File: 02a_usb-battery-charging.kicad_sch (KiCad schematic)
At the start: 22 parts, among them J5 USB4105-GF-A, J8 Conn_01x02_Socket, U3 BQ25170JDSGR

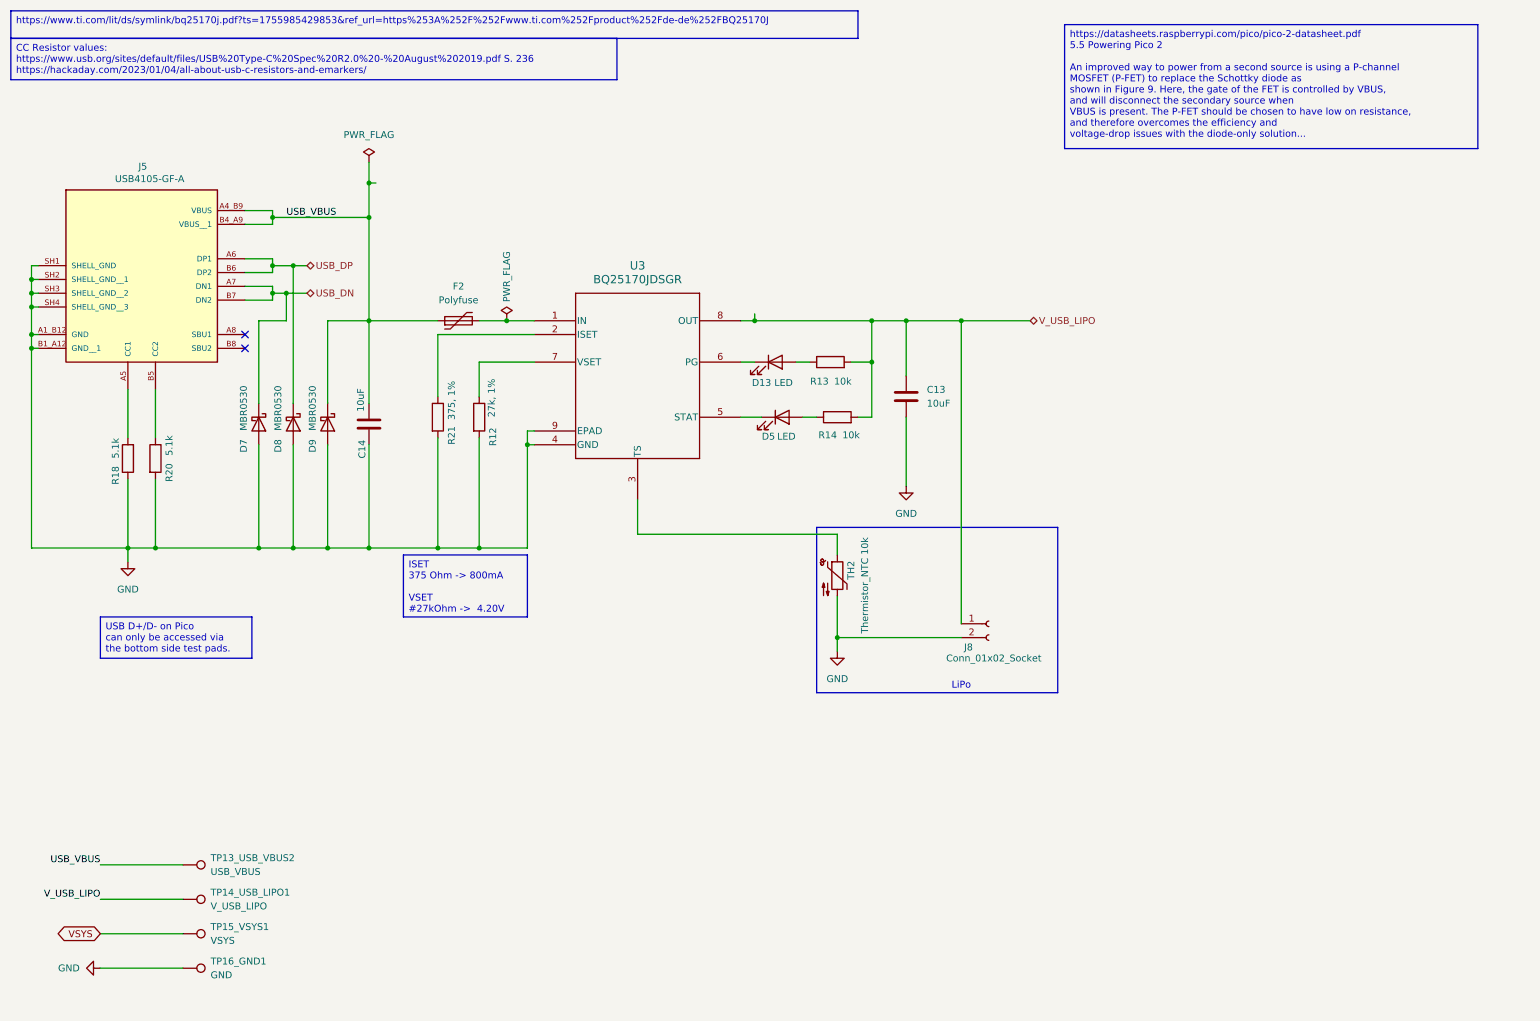
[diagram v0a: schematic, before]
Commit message: v2: major changes
- Move to hierarchical labels
- use another RP Pico Footprint
- split power path in USB/charging and on/off with a button approach in order to control turning on and off
  with the RP Pico, make use of long presses and delay turning of the voltage in order to do a proper shutdown
- introduce another charging controller with a better performance an a lower voltage needed in order to charge the battery
- rework display booster circuit
- rework SD and buttons
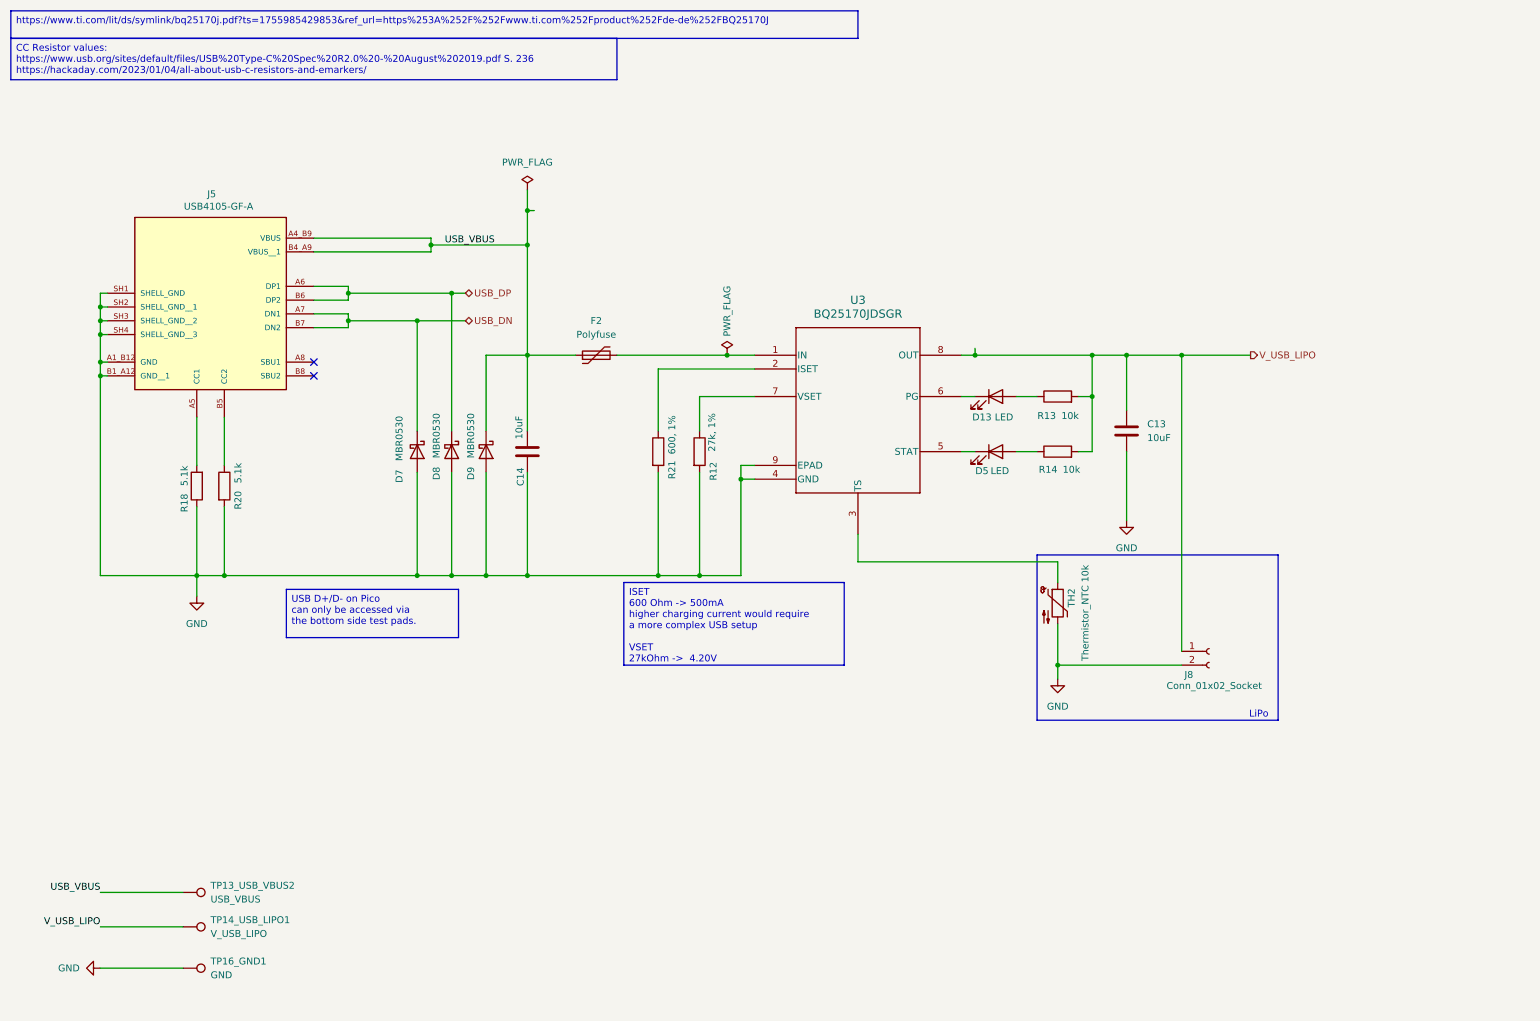
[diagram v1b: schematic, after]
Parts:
- removed TP15_VSYS1: VSYS, TestPoint:TestPoint_Pad_D2.5mm, symbol Connector:TestPoint
- F2: footprint (none) -> Resistor_SMD:R_1206_3216Metric_Pad1.30x1.75mm_HandSolder
- R21: value 375, 1% -> 600, 1%
- U3: footprint WSON8_BQ2517_TEX -> prj-footprints:WSON8_BQ2517_TEX
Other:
- moved on the sheet: C13, C14, D13, D5, D7, D8, D9, F2, J5, J8, R12, R13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

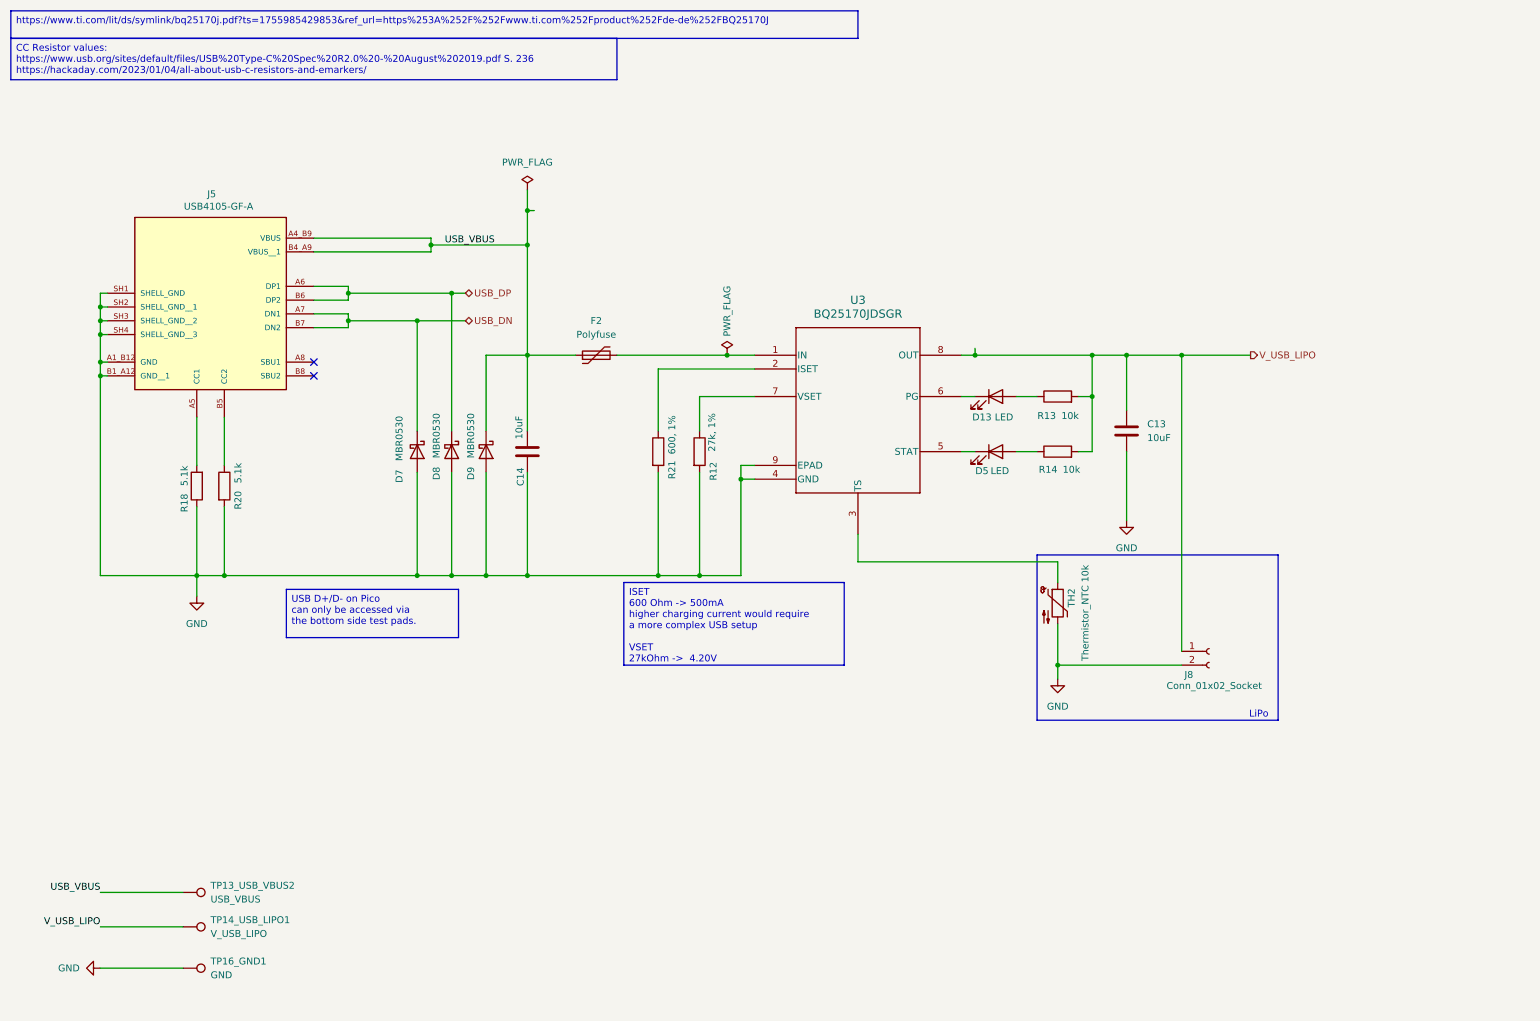
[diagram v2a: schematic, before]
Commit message: Reworked v2 routing
- some general improvements
- reworked component numbering
- routed and tuned differential pair (USB)
- added stiching vias and improved ground fills
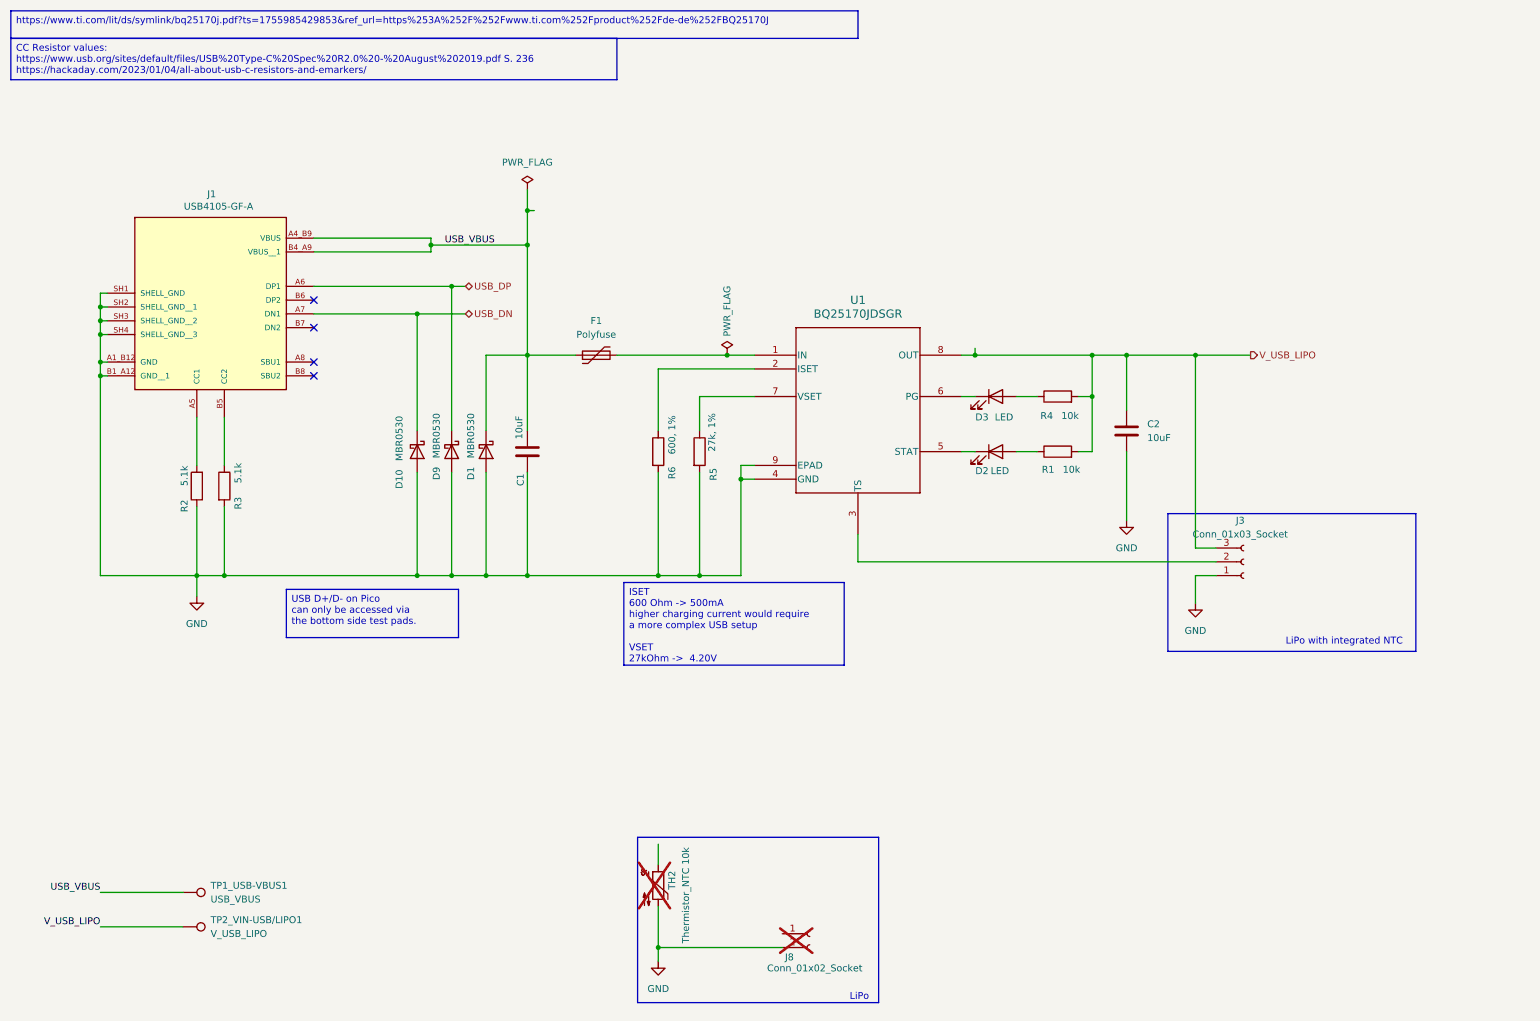
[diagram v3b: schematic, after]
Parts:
- removed TP16_GND1: GND, TestPoint:TestPoint_Pad_D2.5mm, symbol Connector:TestPoint
- added J3: Conn_01x03_Socket, Connector_JST:JST_PH_S3B-PH-K_1x03_P2.00mm_Horizontal, symbol Connector:Conn_01x03_Socket
- J8, TH2: now not fitted; now left out of the parts list
- renumbered C14 to C1, C13 to C2, D9 to D1, D7 to D10, D5 to D2, D13 to D3, D8 to D9, F2 to F1, J5 to J1, R14 to R1, R18 to R2, R20 to R3, R13 to R4, R12 to R5, R21 to R6, TP13_USB_VBUS2 to TP1_USB-VBUS1, TP14_USB_LIPO1 to TP2_VIN-USB/LIPO1, U3 to U1
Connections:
- net GND: now also J3.1 (Pin_1)
- net USB_DN: no longer J1.B7 (DN2)
- net USB_DP: no longer J1.B6 (DP2)
- net V_USB_LIPO: now also J3.3 (Pin_3); no longer J8.1 (Pin_1)
- net at TH2.1: no longer U1.3 (TS)
- new net: J3.2 (Pin_2), U1.3 (TS)
- no-connect marks 2 -> 4
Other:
- note added: "LiPo with integrated NTC"

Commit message: some minor improvements after evaluating the CI run
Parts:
- TP1_USB-VBUS1, TP2_VIN-USB/LIPO1: now left out of the parts list
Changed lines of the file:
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@@
 		(unit 1)
 		(exclude_from_sim no)
-		(in_bom yes)
+		(in_bom no)
 		(on_board yes)
 		(dnp no)
@@
 		(unit 1)
 		(exclude_from_sim no)
-		(in_bom yes)
-		(on_board yes)
-		(dnp no)
+		(in_bom no)
+		(on_board yes)
+		(dnp no)

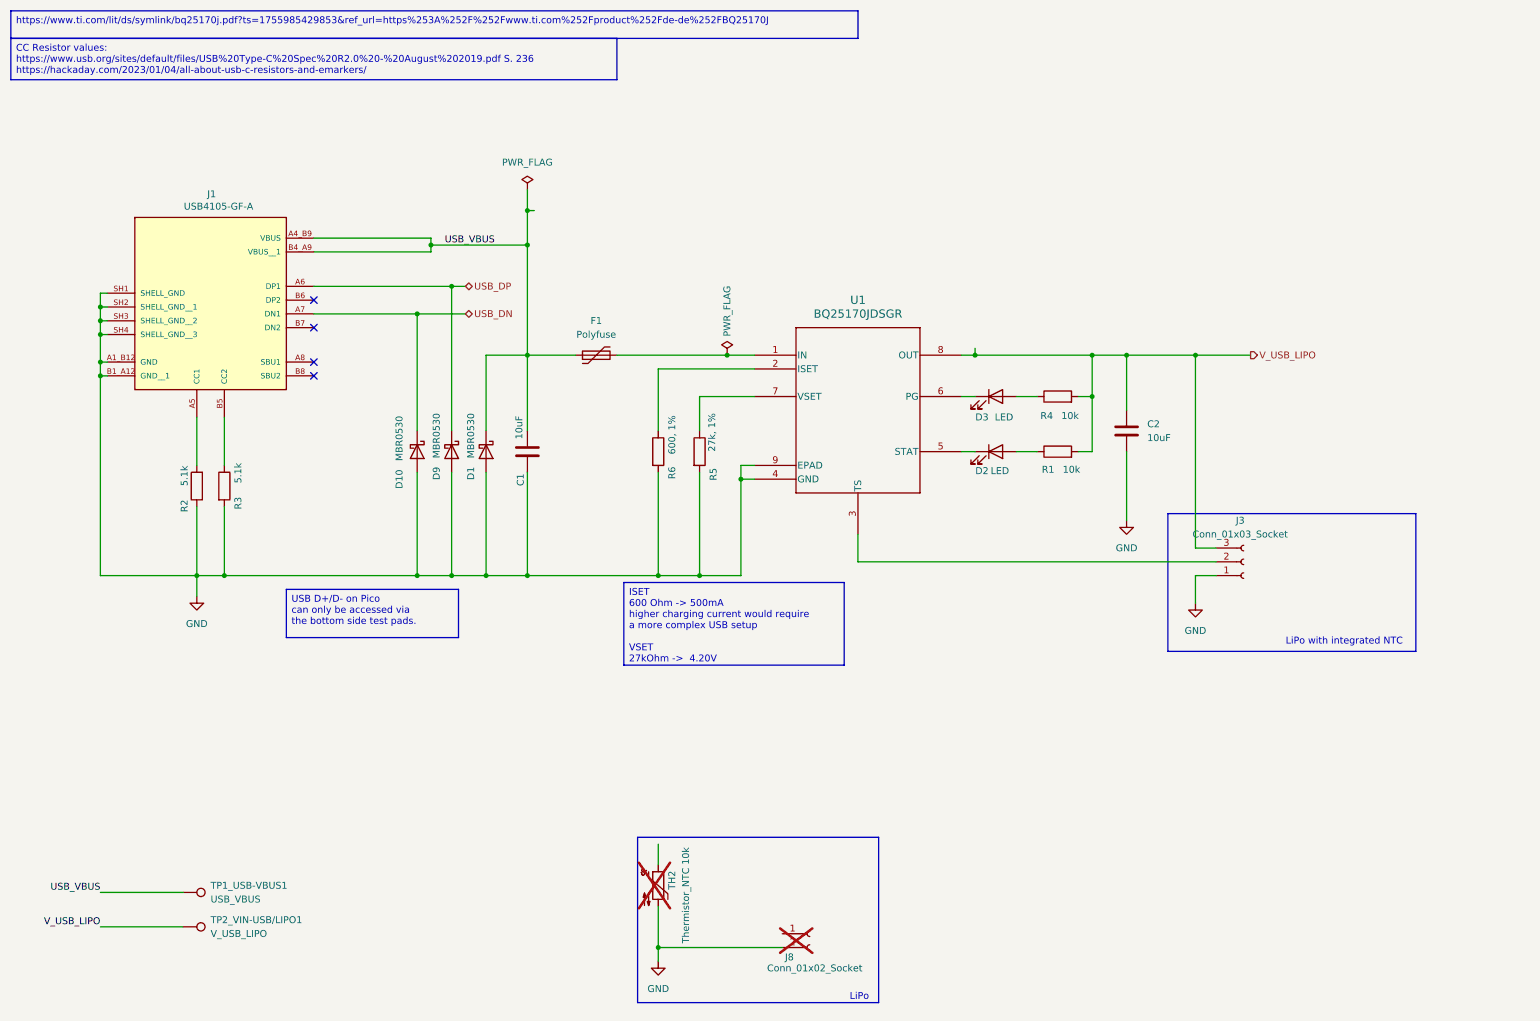
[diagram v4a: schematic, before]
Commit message: v2: final touch
- add proper ESD diodes for USB
- move the USB fuse right after the connector
- pretty labels for test points
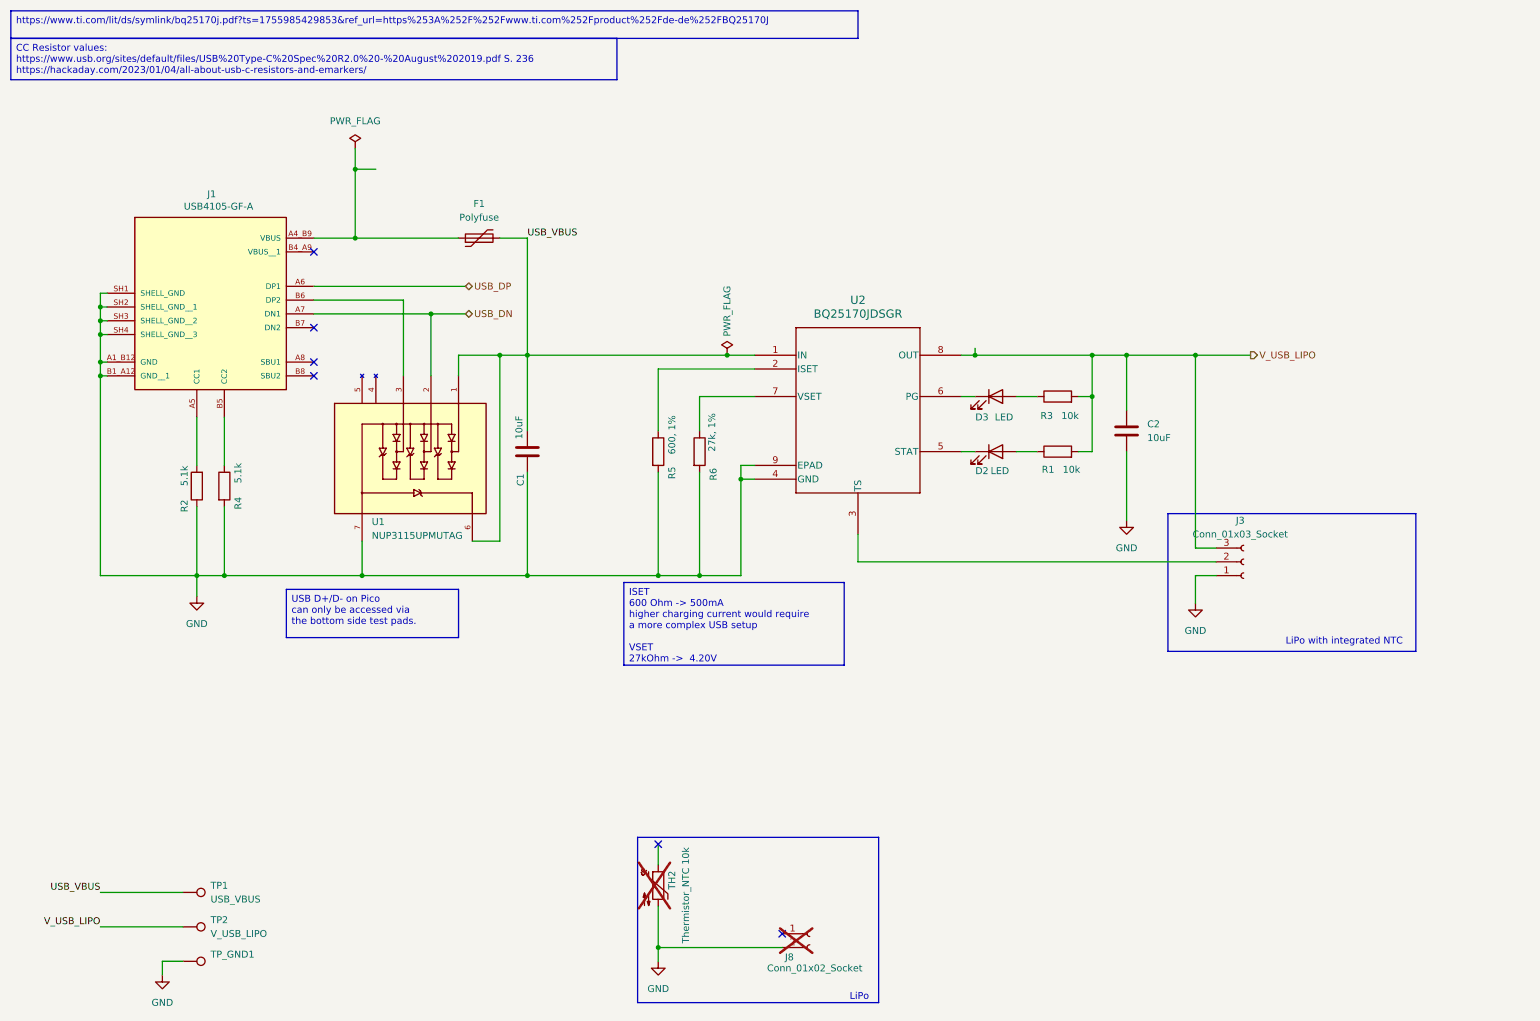
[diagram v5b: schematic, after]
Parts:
- removed D1, D10, D9: MBR0530, Diode_SMD:D_SOD-123, symbol Diode:MBR0530
- added TP_GND1: ~, TestPoint:TestPoint_Pad_D2.5mm, symbol Connector:TestPoint
- added U1: NUP3115UPMUTAG, prj-footprints:UDFN6_1P60X1P60_ONS, symbol NUP3115UPMUTAG:NUP3115UPMUTAG
- renumbered R4 to R3, R3 to R4, R6 to R5, R5 to R6, TP1_USB-VBUS1 to TP1, TP2_VIN-USB/LIPO1 to TP2, U1 to U2
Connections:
- net GND: now also TP_GND1.1, U1.7
- net USB_DN: now also U1.2
- net USB_VBUS: now also F1.2, U2.1 (IN), U1.1, U1.6; no longer F1.1, J1.A4_B9 (VBUS), J1.B4_A9 (VBUS__1)
- net at J1.B6 (DP2): now also U1.3
- new net: F1.1, J1.A4_B9 (VBUS)
- no-connect marks 4 -> 6
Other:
- moved on the sheet: F1
